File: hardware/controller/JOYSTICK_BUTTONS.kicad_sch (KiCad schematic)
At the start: 18 parts, among them SW1 UP, SW2 LEFT, SW3 DOWN, SW4 RIGHT

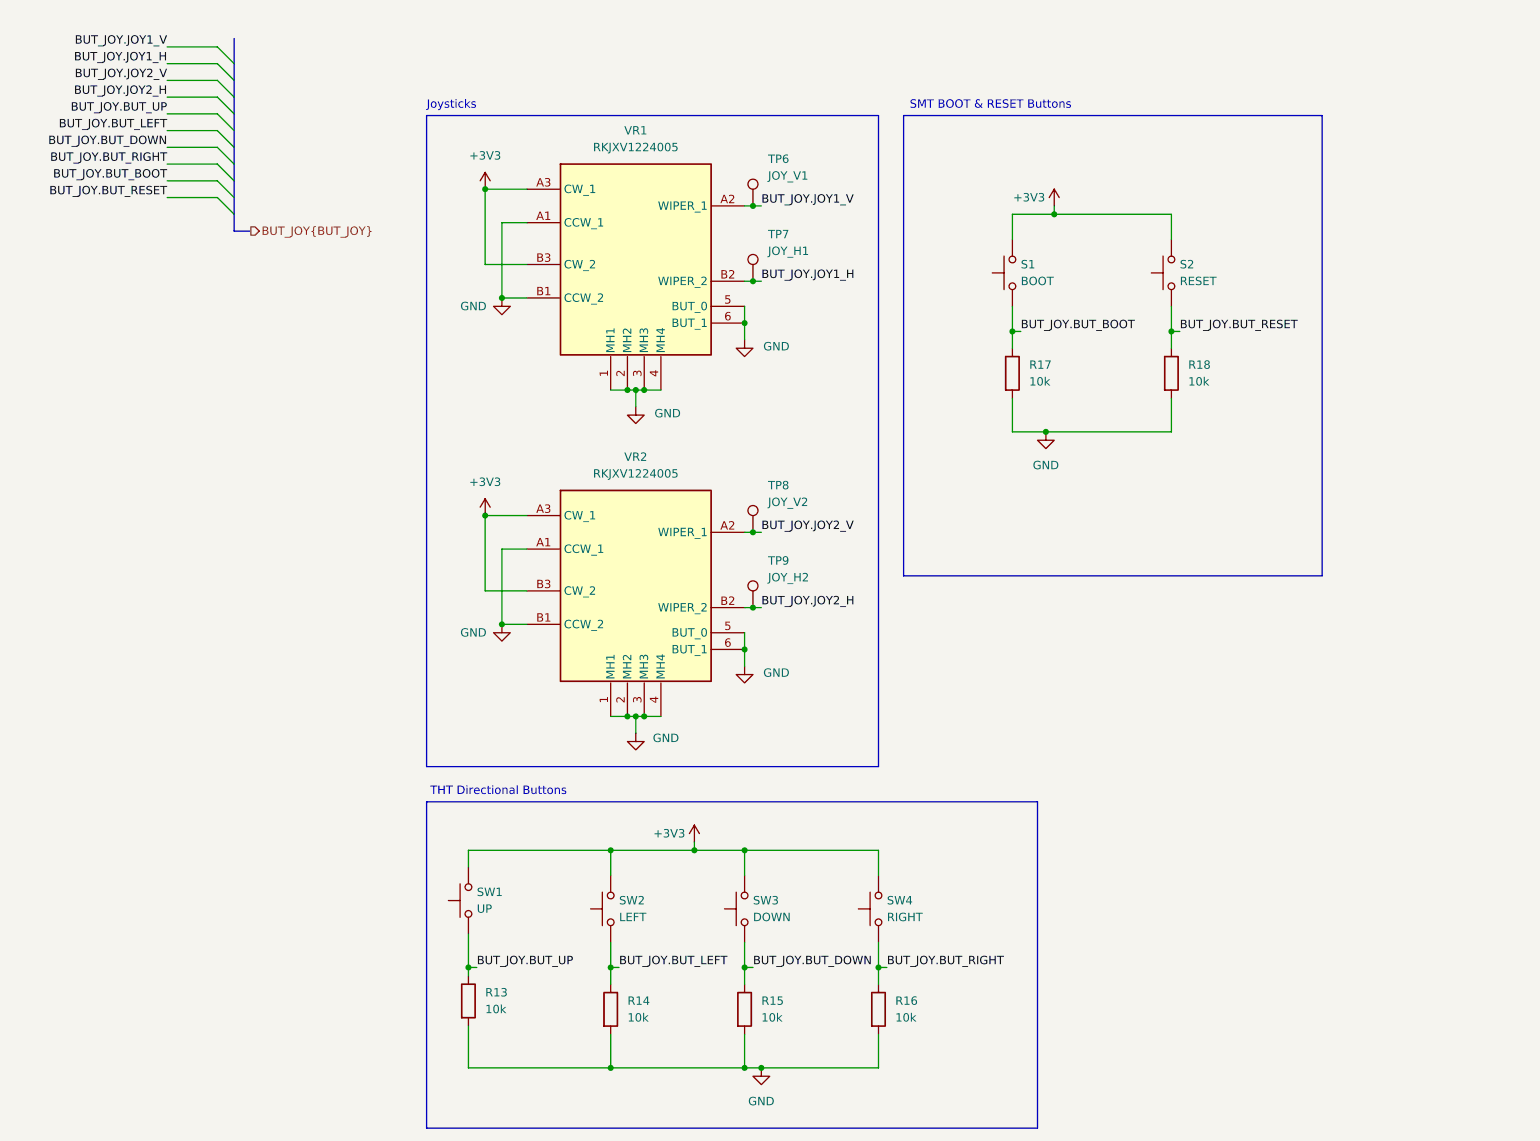
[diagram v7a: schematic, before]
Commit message: ERC good to go. grouped all components on pcb
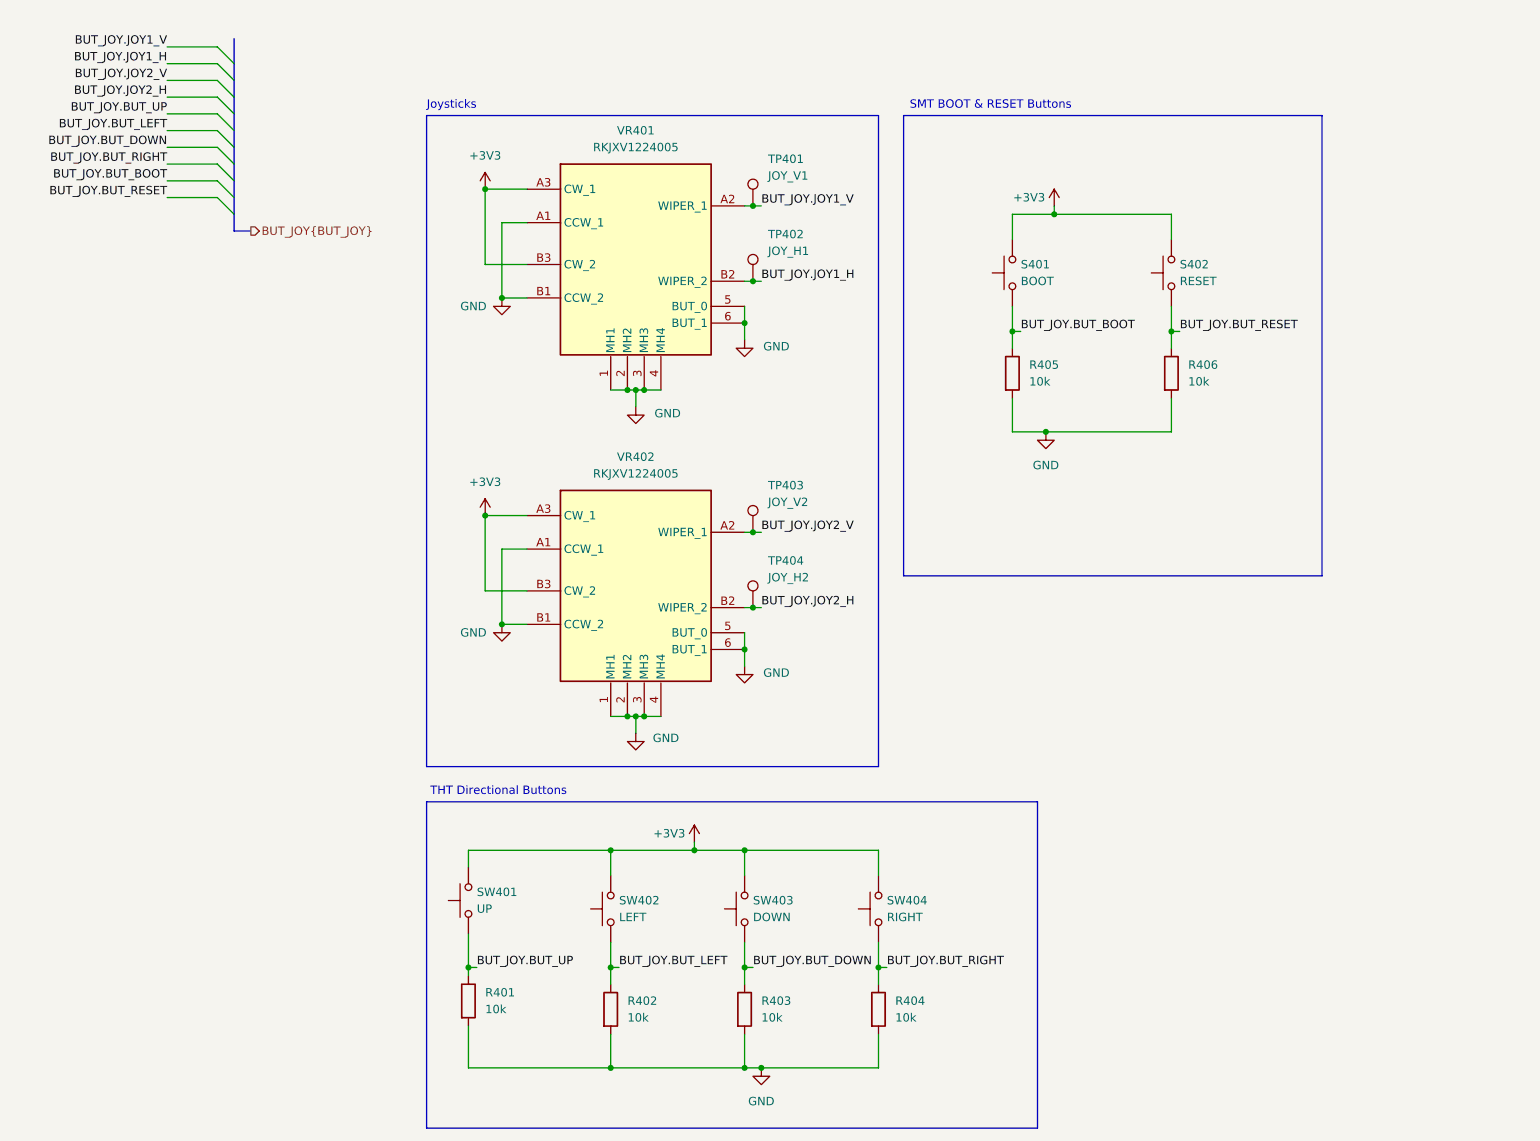
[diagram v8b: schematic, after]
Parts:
- R401: renamed from R13; footprint RESC2012X60N -> SamacSys_Parts:RESC2012X60N
- R402: renamed from R14; footprint RESC2012X60N -> SamacSys_Parts:RESC2012X60N
- R403: renamed from R15; footprint RESC2012X60N -> SamacSys_Parts:RESC2012X60N
- R404: renamed from R16; footprint RESC2012X60N -> SamacSys_Parts:RESC2012X60N
- R405: renamed from R17; footprint RESC2012X60N -> SamacSys_Parts:RESC2012X60N
- R406: renamed from R18; footprint RESC2012X60N -> SamacSys_Parts:RESC2012X60N
- S401: renamed from S1; footprint TL1030AF500AQJ -> SamacSys_Parts:TL1030AF500AQJ
- S402: renamed from S2; footprint TL1030AF500AQJ -> SamacSys_Parts:TL1030AF500AQJ
- VR401: renamed from VR1; footprint RKJXV1224005 -> SamacSys_Parts:RKJXV1224005
- VR402: renamed from VR2; footprint RKJXV1224005 -> SamacSys_Parts:RKJXV1224005
- renumbered SW1 to SW401, SW2 to SW402, SW3 to SW403, SW4 to SW404, TP6 to TP401, TP7 to TP402, TP8 to TP403, TP9 to TP404
